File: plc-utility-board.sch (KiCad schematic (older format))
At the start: 11 parts, among them J1 Screw_Terminal_01x02, J10 Screw_Terminal_01x03, J11 Screw_Terminal_01x02, J2 Screw_Terminal_01x08, J3 Screw_Terminal_01x04, J4 Screw_Terminal_01x08, J5 TerminalBlock_02x04, J6 Conn_01x03_Male, J7 Conn_01x03_Male, J8 Screw_Terminal_01x03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

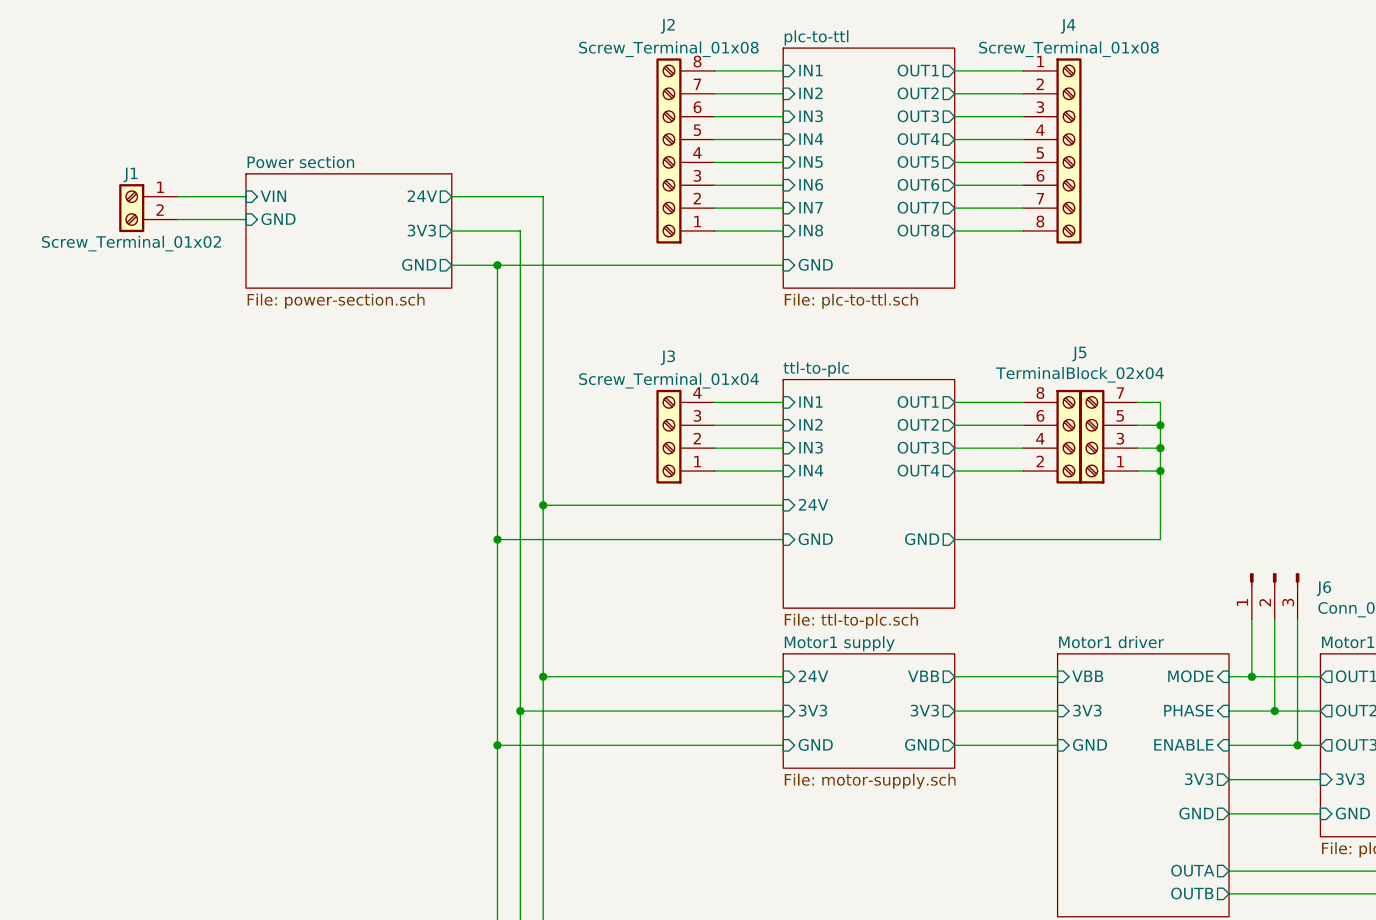
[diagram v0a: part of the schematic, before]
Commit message: PCB creation, improvements of power supply section
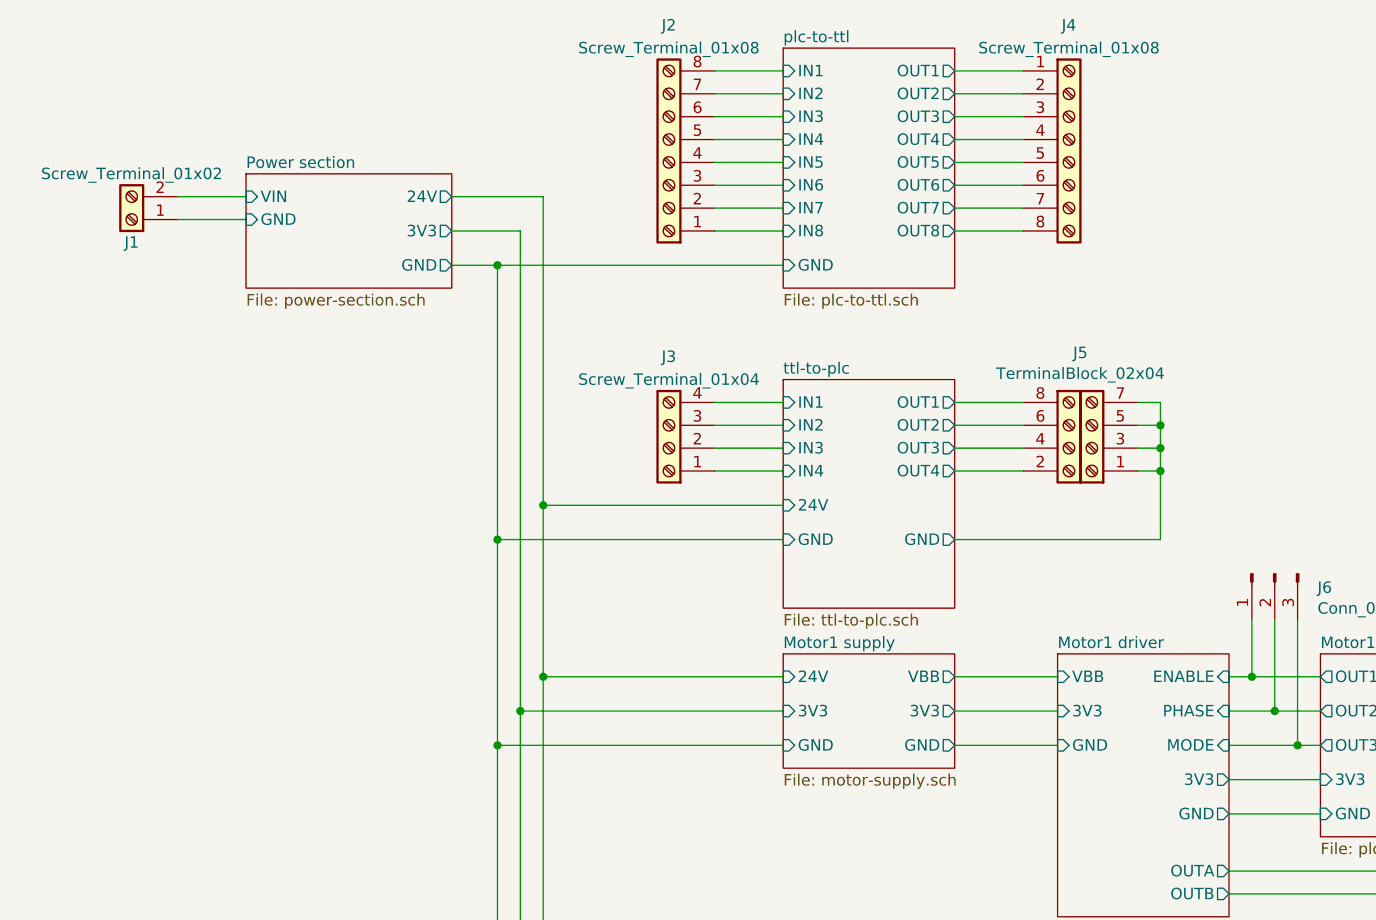
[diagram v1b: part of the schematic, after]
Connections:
- net Power section/GND: now also J1.1 (Pin_1); no longer J1.2 (Pin_2)
- net Power section/VIN: now also J1.2 (Pin_2); no longer J1.1 (Pin_1)
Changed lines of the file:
@@
 L Connector:Screw_Terminal_01x02 J1
 U 1 1 5BF6D1F4
-P 1250 1500
-F 0 "J1" H 1250 1600 50  0000 C CNN
-F 1 "Screw_Terminal_01x02" H 1250 1300 50  0000 C CNN
-F 2 "TerminalBlock:TerminalBlock_bornier-2_P5.08mm" H 1250 1500 50  0001 C CNN
-F 3 "~" H 1250 1500 50  0001 C CNN
-	1    1250 1500
-	-1   0    0    -1
+P 1250 1600
+F 0 "J1" H 1250 1700 50  0000 C CNN
+F 1 "Screw_Terminal_01x02" H 1250 1400 50  0000 C CNN
+F 2 "TerminalBlock:TerminalBlock_bornier-2_P5.08mm" H 1250 1600 50  0001 C CNN
+F 3 "~" H 1250 1600 50  0001 C CNN
+	1    1250 1600
+	-1   0    0    1
 $EndComp
 Wire Wire Line
@@
 F3 "3V3" I L 5300 3750 50
 F4 "GND" I L 5300 3900 50
-F5 "MODE" I R 6050 3600 50
+F5 "MODE" I R 6050 3900 50
 F6 "PHASE" I R 6050 3750 50
-F7 "ENABLE" I R 6050 3900 50
+F7 "ENABLE" I R 6050 3600 50
 F8 "3V3" O R 6050 4050 50
 F9 "GND" O R 6050 4200 50

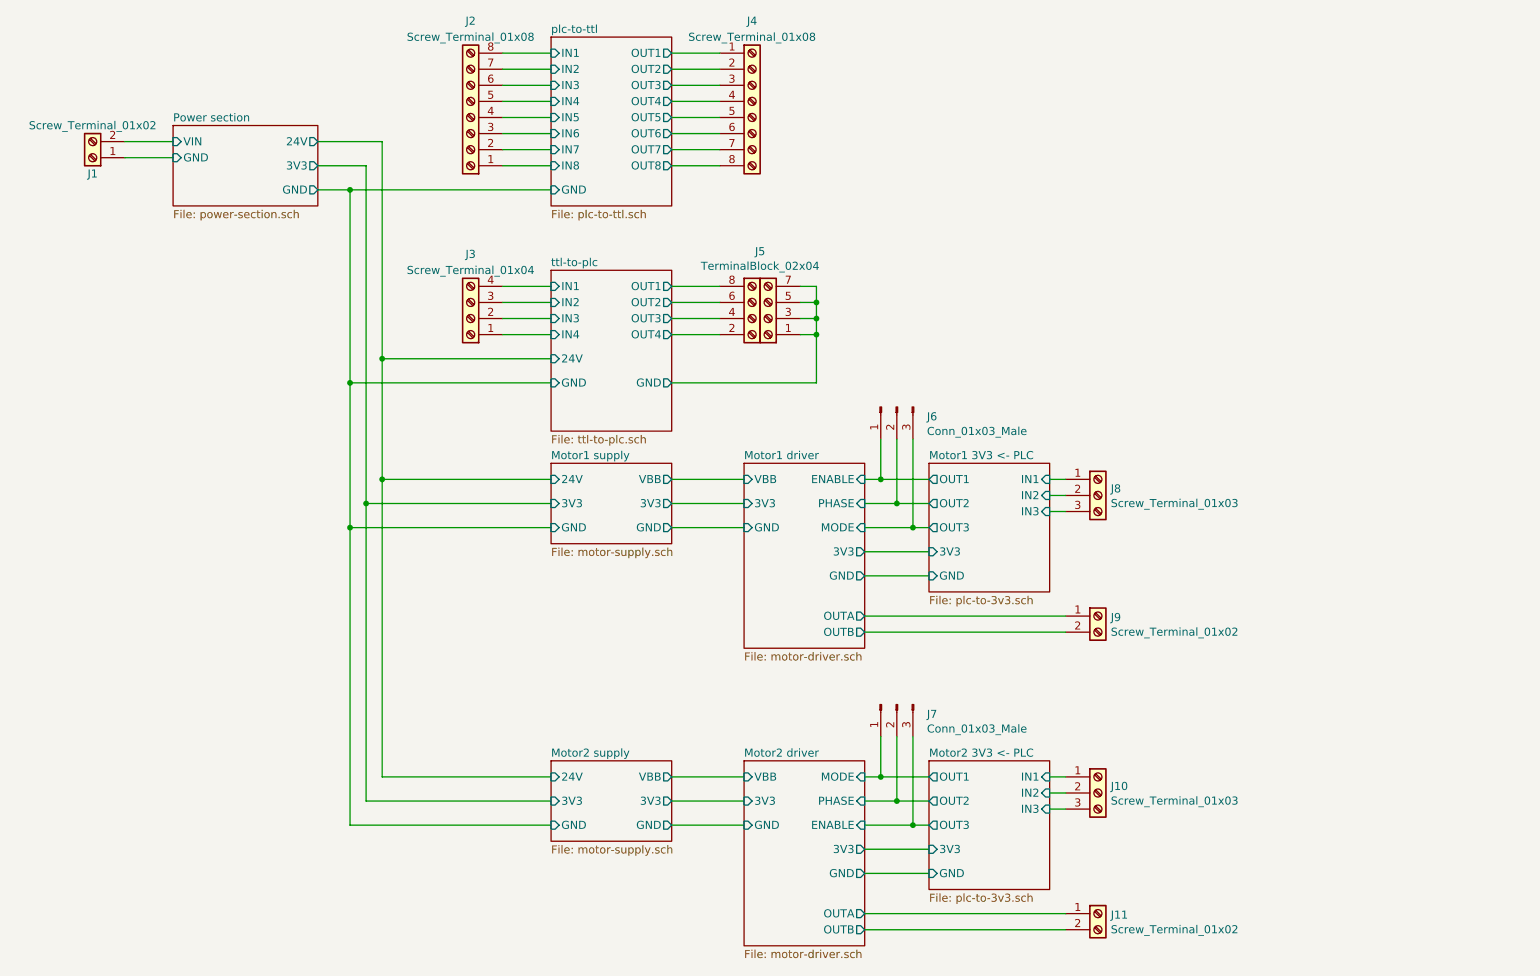
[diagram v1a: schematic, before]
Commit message: Changed Motor Controller to DRV8840, removed pre-motor power section. Replaced PNP transistors in logic level shifters with P-MOSFET units
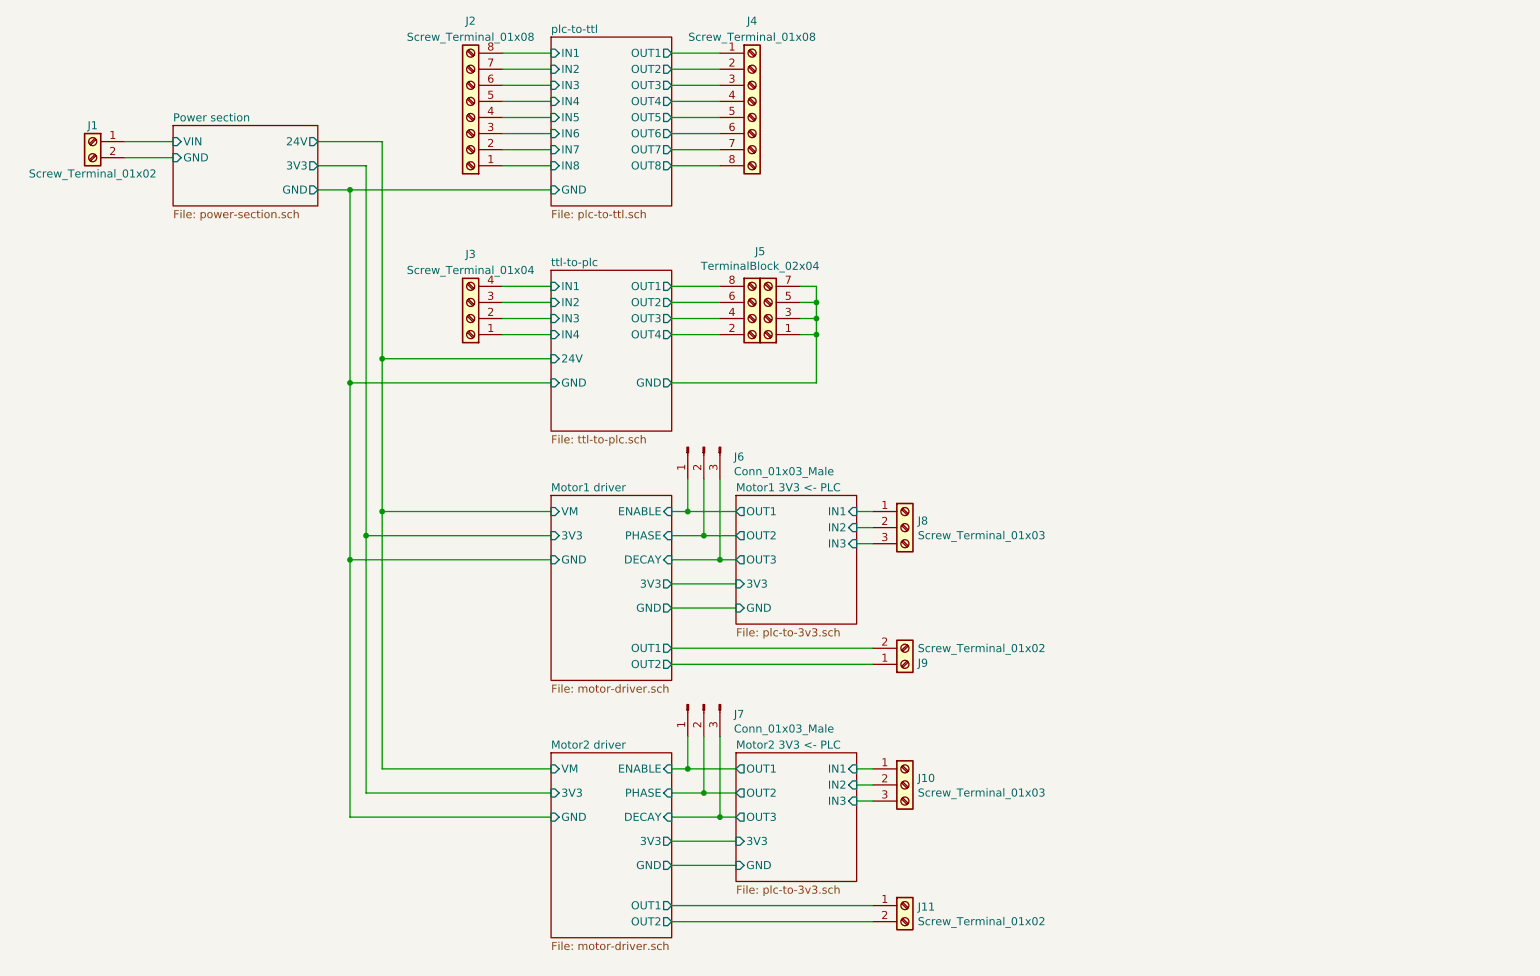
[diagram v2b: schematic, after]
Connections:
- net Power section/GND: now also J1.2 (Pin_2); no longer J1.1 (Pin_1)
- net Power section/VIN: now also J1.1 (Pin_1); no longer J1.2 (Pin_2)
- net Motor1 driver/OUTA renamed Motor1 driver/OUT2
- net Motor1 driver/OUTB renamed Motor1 driver/OUT1
- net Motor2 driver/OUTA renamed Motor2 driver/OUT1
- net Motor2 driver/OUTB renamed Motor2 driver/OUT2
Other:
- moved on the sheet: J10, J11, J6, J7, J8, J9

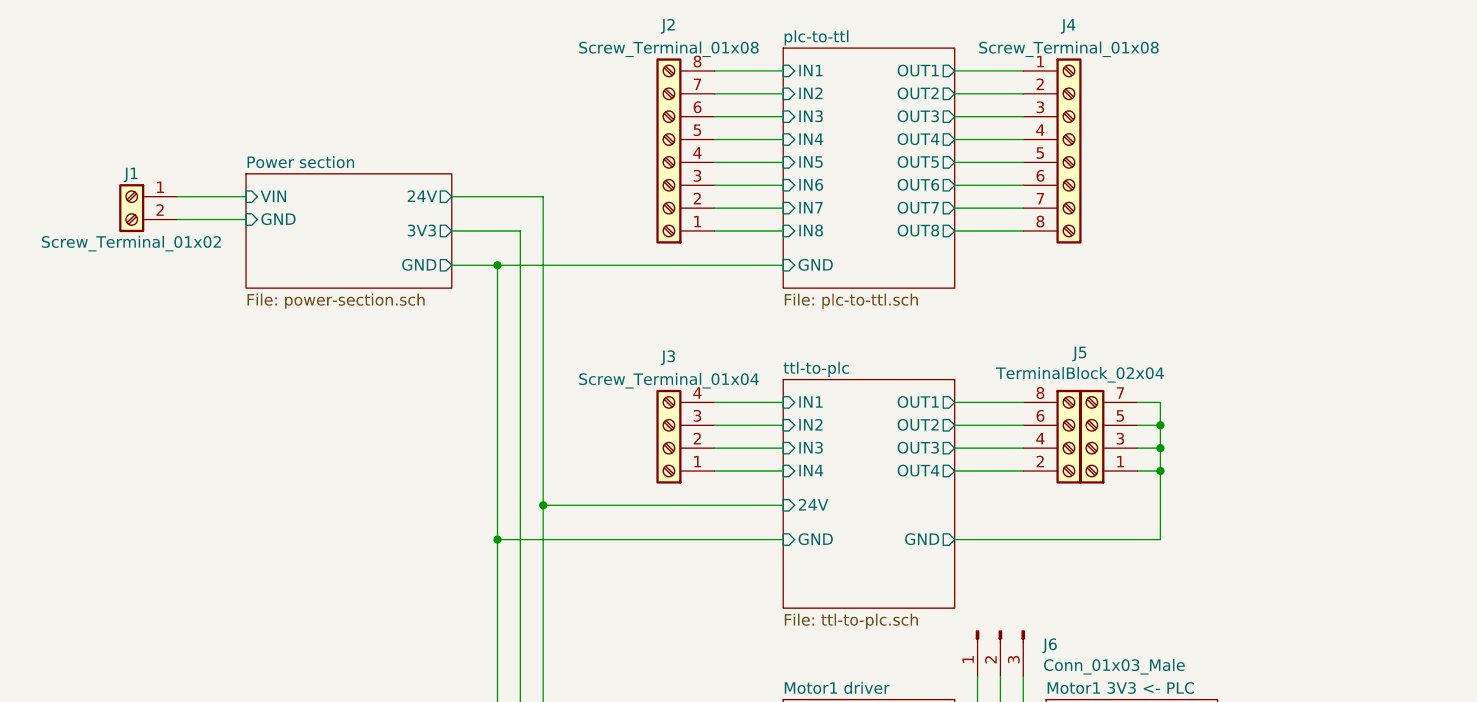
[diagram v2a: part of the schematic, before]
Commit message: Re-placed components of 3.3->24V converter. Improvement placement of Motor Controller components
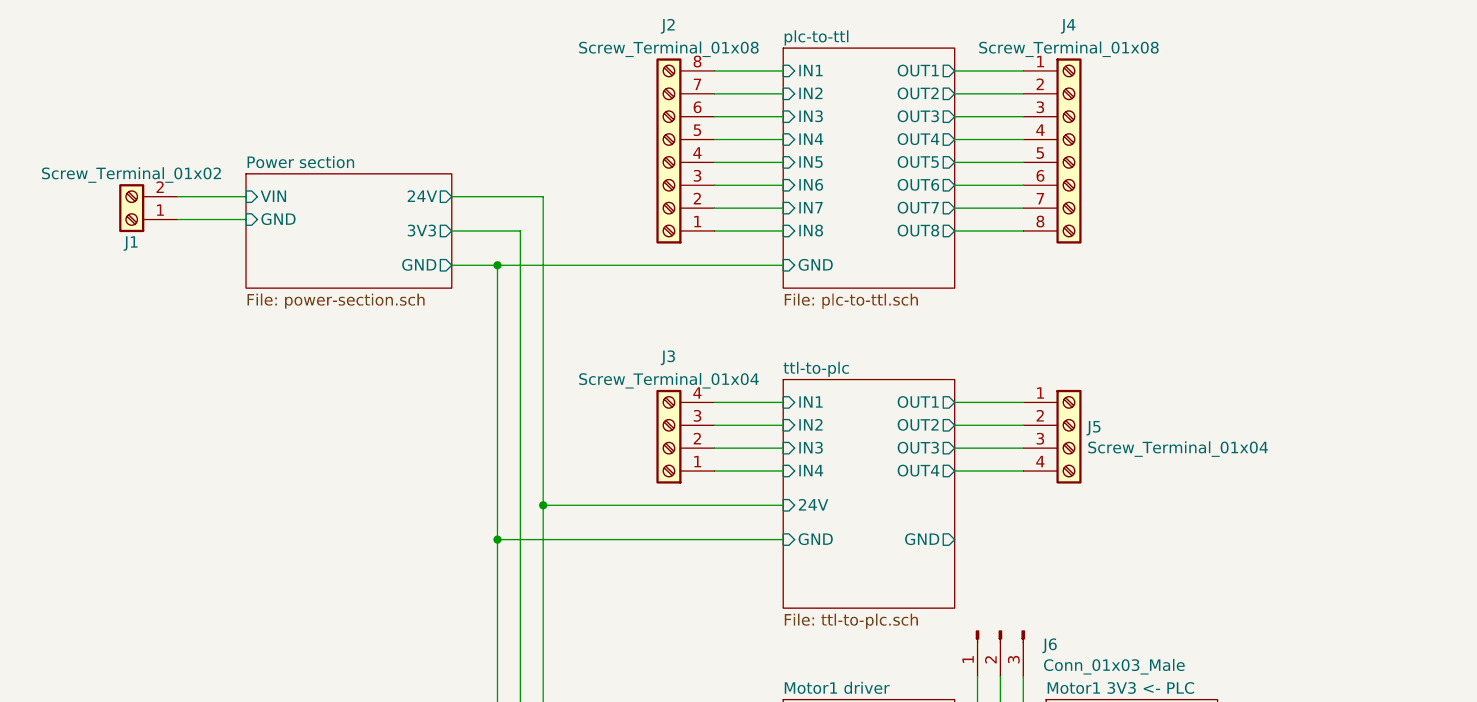
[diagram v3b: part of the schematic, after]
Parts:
- removed J5: TerminalBlock_02x04, mylib:DG500B-5.0-4P14, symbol mylib:TerminalBlock_02x04
- added J5: Screw_Terminal_01x04, TerminalBlock_Phoenix:TerminalBlock_Phoenix_MKDS-1,5-4-5.08_1x04_P5.08mm_Horizontal, symbol mylib:Screw_Terminal_01x04
- J1: footprint TerminalBlock:TerminalBlock_bornier-2_P5.08mm -> TerminalBlock_Phoenix:TerminalBlock_Phoenix_MKDS-1,5-2-5.08_1x02_P5.08mm_Horizontal
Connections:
- net Power section/GND: now also J1.1 (Pin_1); no longer J1.2 (Pin_2)
- net Power section/VIN: now also J1.2 (Pin_2); no longer J1.1 (Pin_1)
- net ttl-to-plc/OUT1: now also J5.1 (Pin_1)
- net ttl-to-plc/OUT2: now also J5.2 (Pin_2)
- net ttl-to-plc/OUT3: now also J5.3 (Pin_3)
- net ttl-to-plc/OUT4: now also J5.4 (Pin_4)
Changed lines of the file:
@@
 L Connector:Screw_Terminal_01x02 J1
 U 1 1 5BF6D1F4
-P 1250 1500
-F 0 "J1" H 1250 1600 50  0000 C CNN
-F 1 "Screw_Terminal_01x02" H 1250 1300 50  0000 C CNN
-F 2 "TerminalBlock:TerminalBlock_bornier-2_P5.08mm" H 1250 1500 50  0001 C CNN
-F 3 "~" H 1250 1500 50  0001 C CNN
-	1    1250 1500
-	-1   0    0    -1
+P 1250 1600
+F 0 "J1" H 1250 1700 50  0000 C CNN
+F 1 "Screw_Terminal_01x02" H 1250 1400 50  0000 C CNN
+F 2 "TerminalBlock_Phoenix:TerminalBlock_Phoenix_MKDS-1,5-2-5.08_1x02_P5.08mm_Horizontal" H 1250 1600 50  0001 C CNN
+F 3 "~" H 1250 1600 50  0001 C CNN
+	1    1250 1600
+	-1   0    0    1
 $EndComp
 Wire Wire Line
@@
 Wire Wire Line
 	4850 2400 5150 2400
-$Comp
-L mylib:TerminalBlock_02x04 J5
-U 1 1 5BE0B666
-P 5400 2600
-F 0 "J5" H 5400 2183 50  0000 C CNN
-F 1 "TerminalBlock_02x04" H 5400 2274 50  0000 C CNN
-F 2 "mylib:DG500B-5.0-4P14" H 5400 2600 50  0001 C CNN
-F 3 "" H 5400 2600 50  0001 C CNN
-	1    5400 2600
-	-1   0    0    1
-$EndComp
 Wire Wire Line
 	4850 2500 5150 2500
@@
 Wire Wire Line
 	5150 2700 4850 2700
-Wire Wire Line
-	4850 3000 5750 3000
-Wire Wire Line
-	5750 3000 5750 2700
-Wire Wire Line
-	5750 2400 5650 2400
-Wire Wire Line
-	5650 2500 5750 2500
-Connection ~ 5750 2500
-Wire Wire Line
-	5750 2500 5750 2400
-Wire Wire Line
-	5650 2600 5750 2600
-Connection ~ 5750 2600
-Wire Wire Line
-	5750 2600 5750 2500
-Wire Wire Line
-	5650 2700 5750 2700
-Connection ~ 5750 2700
-Wire Wire Line
-	5750 2700 5750 2600
 Wire Wire Line
 	3050 2850 3050 3800
@@
 Wire Wire Line
 	2850 4100 2850 5700
+$Comp
+L mylib:Screw_Terminal_01x04 J5
+U 1 1 5BEF4585
+P 5350 2500
+F 0 "J5" H 5430 2492 50  0000 L CNN
+F 1 "Screw_Terminal_01x04" H 5430 2401 50  0000 L CNN
+F 2 "TerminalBlock_Phoenix:TerminalBlock_Phoenix_MKDS-1,5-4-5.08_1x04_P5.08mm_Horizontal" H 5350 2500 50  0001 C CNN
+F 3 "~" H 5350 2500 50  0001 C CNN
+	1    5350 2500
+	1    0    0    -1
+$EndComp
 $EndSCHEMATC

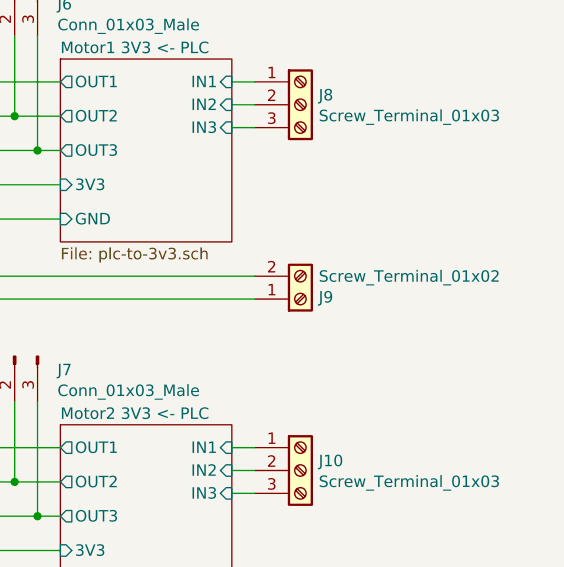
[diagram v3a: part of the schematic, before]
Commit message: Routed all nets without GND. Added logo
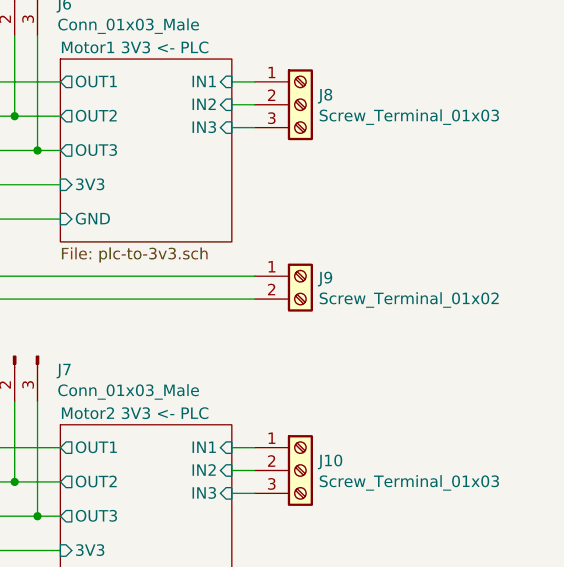
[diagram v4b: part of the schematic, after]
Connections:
- net Motor1 driver/OUT1: now also J9.1 (Pin_1); no longer J9.2 (Pin_2)
- net Motor1 driver/OUT2: now also J9.2 (Pin_2); no longer J9.1 (Pin_1)
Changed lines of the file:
@@
 L Connector:Screw_Terminal_01x02 J9
 U 1 1 5BE7A1DF
-P 6300 4750
-F 0 "J9" H 6380 4742 50  0000 L CNN
-F 1 "Screw_Terminal_01x02" H 6380 4651 50  0000 L CNN
-F 2 "TerminalBlock_Phoenix:TerminalBlock_Phoenix_MKDS-1,5-2-5.08_1x02_P5.08mm_Horizontal" H 6300 4750 50  0001 C CNN
-F 3 "~" H 6300 4750 50  0001 C CNN
-	1    6300 4750
-	1    0    0    1
+P 6300 4650
+F 0 "J9" H 6380 4642 50  0000 L CNN
+F 1 "Screw_Terminal_01x02" H 6380 4551 50  0000 L CNN
+F 2 "TerminalBlock_Phoenix:TerminalBlock_Phoenix_MKDS-1,5-2-5.08_1x02_P5.08mm_Horizontal" H 6300 4650 50  0001 C CNN
+F 3 "~" H 6300 4650 50  0001 C CNN
+	1    6300 4650
+	1    0    0    -1
 $EndComp
 Wire Wire Line
